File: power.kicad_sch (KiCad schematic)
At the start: 25 parts, among them U1 ECP5U_12_CABGA256, U2 TLV62569DBV, U3 TLV62569DBV, U4 TLV62569DBV

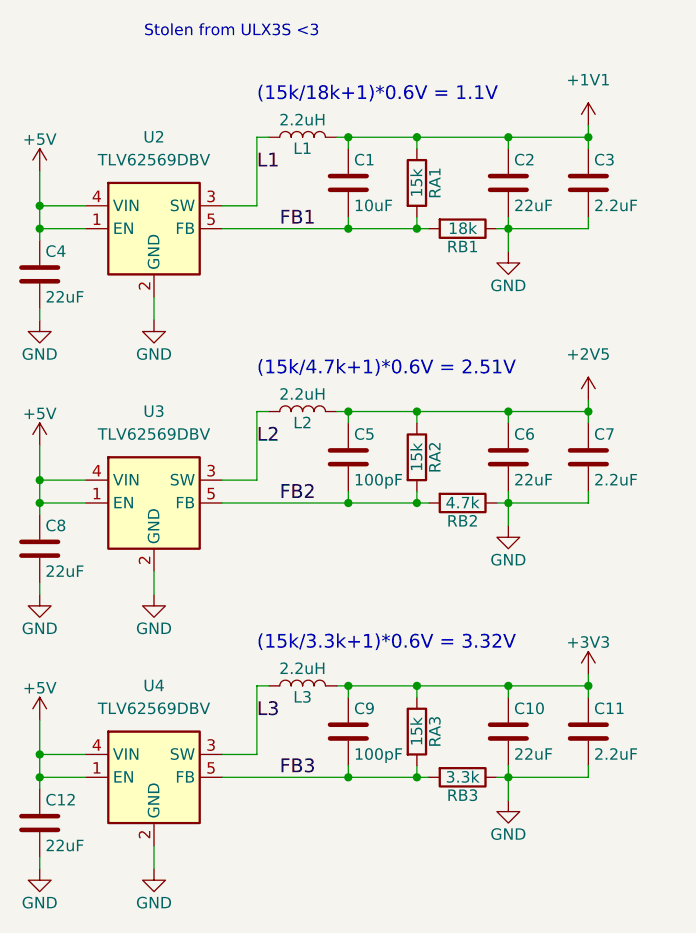
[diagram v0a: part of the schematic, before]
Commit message: Routed HDMI, usb, rotated chip and more
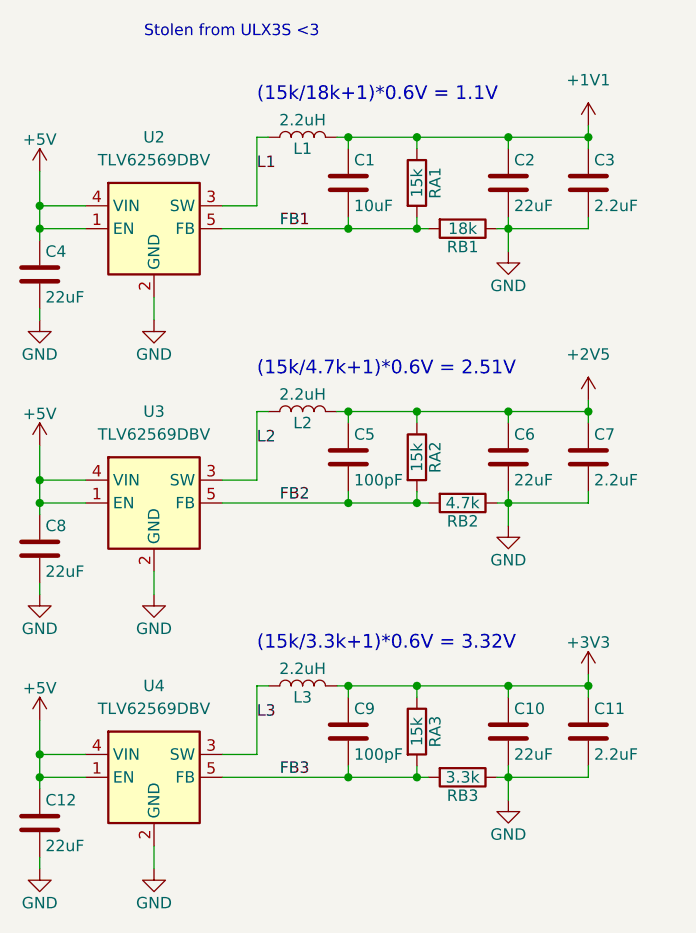
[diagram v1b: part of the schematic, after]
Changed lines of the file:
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@@
 		(effects
 			(font
-				(size 1.524 1.524)
+				(size 1.27 1.27)
 			)
 			(justify left bottom)
@@
 		(effects
 			(font
-				(size 1.524 1.524)
+				(size 1.27 1.27)
 			)
 			(justify left bottom)
@@
 		(effects
 			(font
-				(size 1.524 1.524)
+				(size 1.27 1.27)
 			)
 			(justify left bottom)
@@
 		(effects
 			(font
-				(size 1.524 1.524)
+				(size 1.27 1.27)
 			)
 			(justify left bottom)
@@
 		(effects
 			(font
-				(size 1.524 1.524)
+				(size 1.27 1.27)
 			)
 			(justify left bottom)
@@
 		(effects
 			(font
-				(size 1.524 1.524)
+				(size 1.27 1.27)
 			)
 			(justify left bottom)

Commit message: Stash
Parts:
- removed C1: 10uF, Capacitor_SMD:C_0603_1608Metric, symbol Device:C
- removed C5: 100pF, Capacitor_SMD:C_0603_1608Metric, symbol Device:C
- removed C6: 22uF, Capacitor_SMD:C_0603_1608Metric, symbol Device:C
- removed C7: 2.2uF, Capacitor_SMD:C_0603_1608Metric, symbol Device:C
- removed U2, U3, U4: TLV62569DBV, Package_TO_SOT_SMD:SOT-23-5, symbol Regulator_Switching:TLV62569DBV
- added C27, C29: 100pF, Capacitor_SMD:C_0603_1608Metric, symbol Device:C
- added C28: 10uF, Capacitor_SMD:C_0603_1608Metric, symbol Device:C
- added C36, C37, C38, C42: 100nF, Capacitor_SMD:C_0402_1005Metric, symbol Device:C
- added U12, U13, U14: TLV62569DRL, Package_TO_SOT_SMD:SOT-563, symbol Regulator_Switching:TLV62569DRL
- C10: value 22uF -> 100pF
- C11, C3: value 2.2uF -> 10uF
- C12, C2, C4, C8: value 22uF -> 10uF
- C9: value 100pF -> 10uF
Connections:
- net +1V1: now also C28.1, C29.1, C36.1, C37.1, C38.1, C42.1
- net +2V5: now also C11.1, C27.1
- net +3V3: no longer C11.1
- net +5V: now also U12.3 (VIN), U12.5 (EN), U13.3 (VIN), U13.5 (EN), U14.3 (VIN), U14.5 (EN)
- net FB1: now also U14.1 (FB)
- net FB2: now also U13.1 (FB)
- net FB3: now also U12.1 (FB); no longer C9.2
- net GND: now also C9.2, C27.2, C28.2, C29.2, C36.2, C37.2, C38.2, C42.2, U12.2 (GND), U13.2 (GND), U14.2 (GND)
- net L1: now also U14.4 (SW)
- net L2: now also U13.4 (SW)
- net L3: now also U12.4 (SW)
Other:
- note added: "Inspired from ULX3S <3"
- note removed: "Stolen from ULX3S <3"
- moved on the sheet: C10, C12, C4, C8, C9, L1, L2, L3, RA1, RA2, RA3, RB1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
